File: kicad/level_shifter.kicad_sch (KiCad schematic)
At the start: 22 parts, among them U3 74LVC2T45GT, U4 74LVC2T45GT, U5 74LVC2T45GT

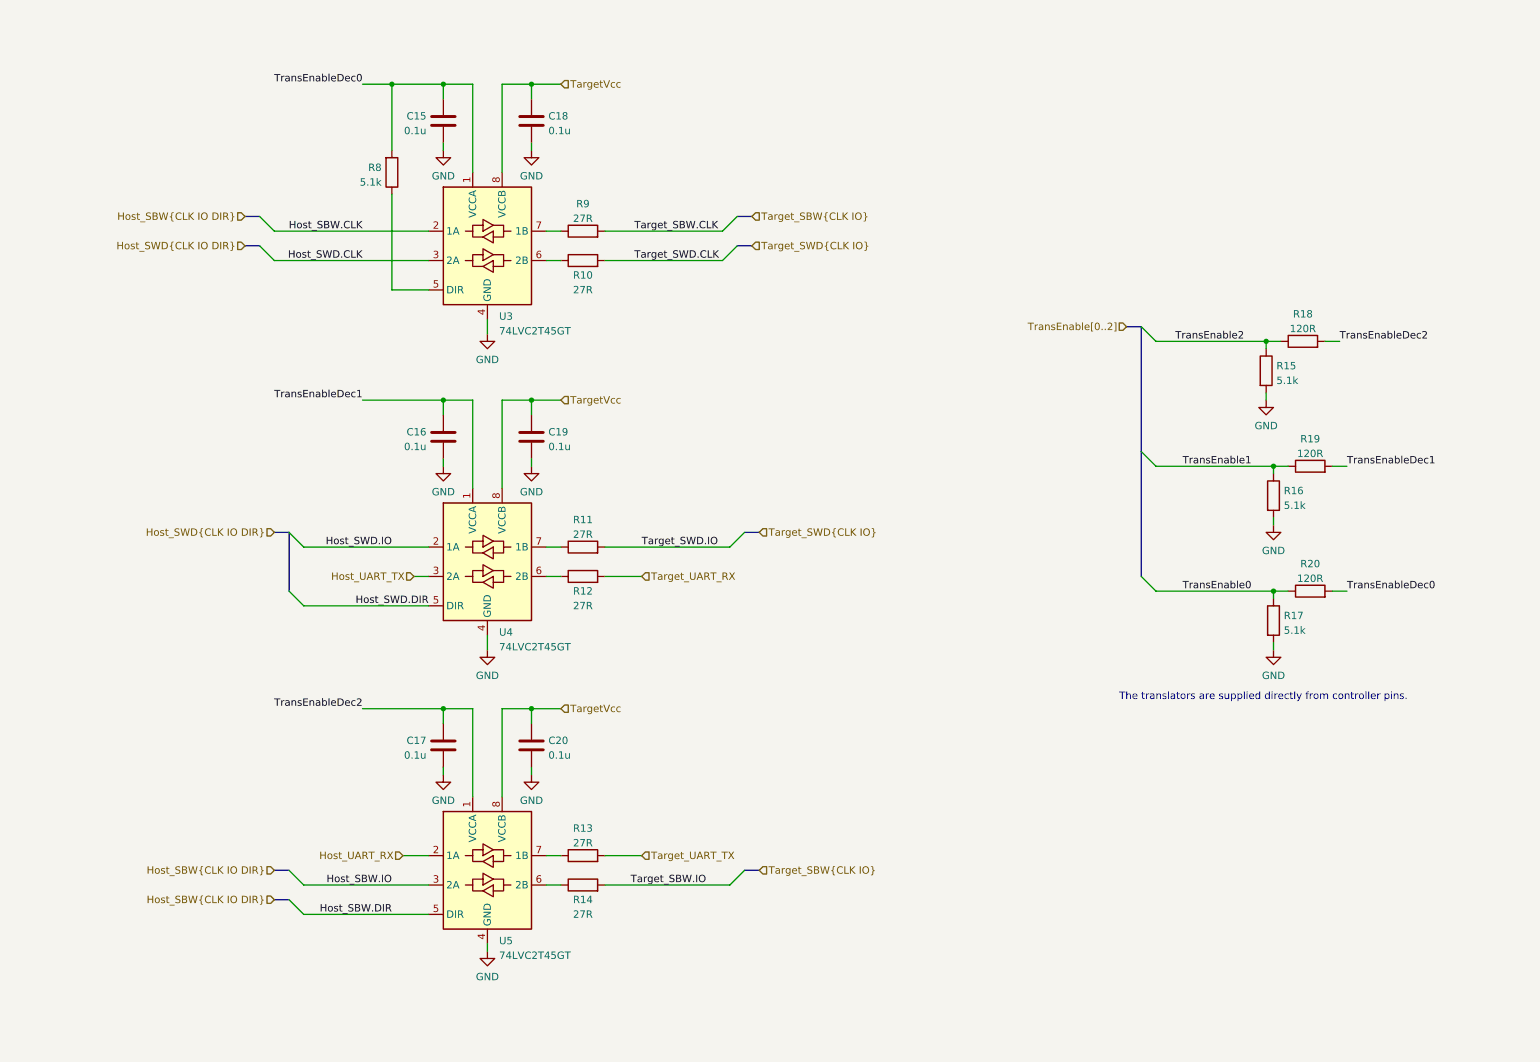
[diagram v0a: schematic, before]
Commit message: add fourth level converter for simultaneous programming + TX/RX
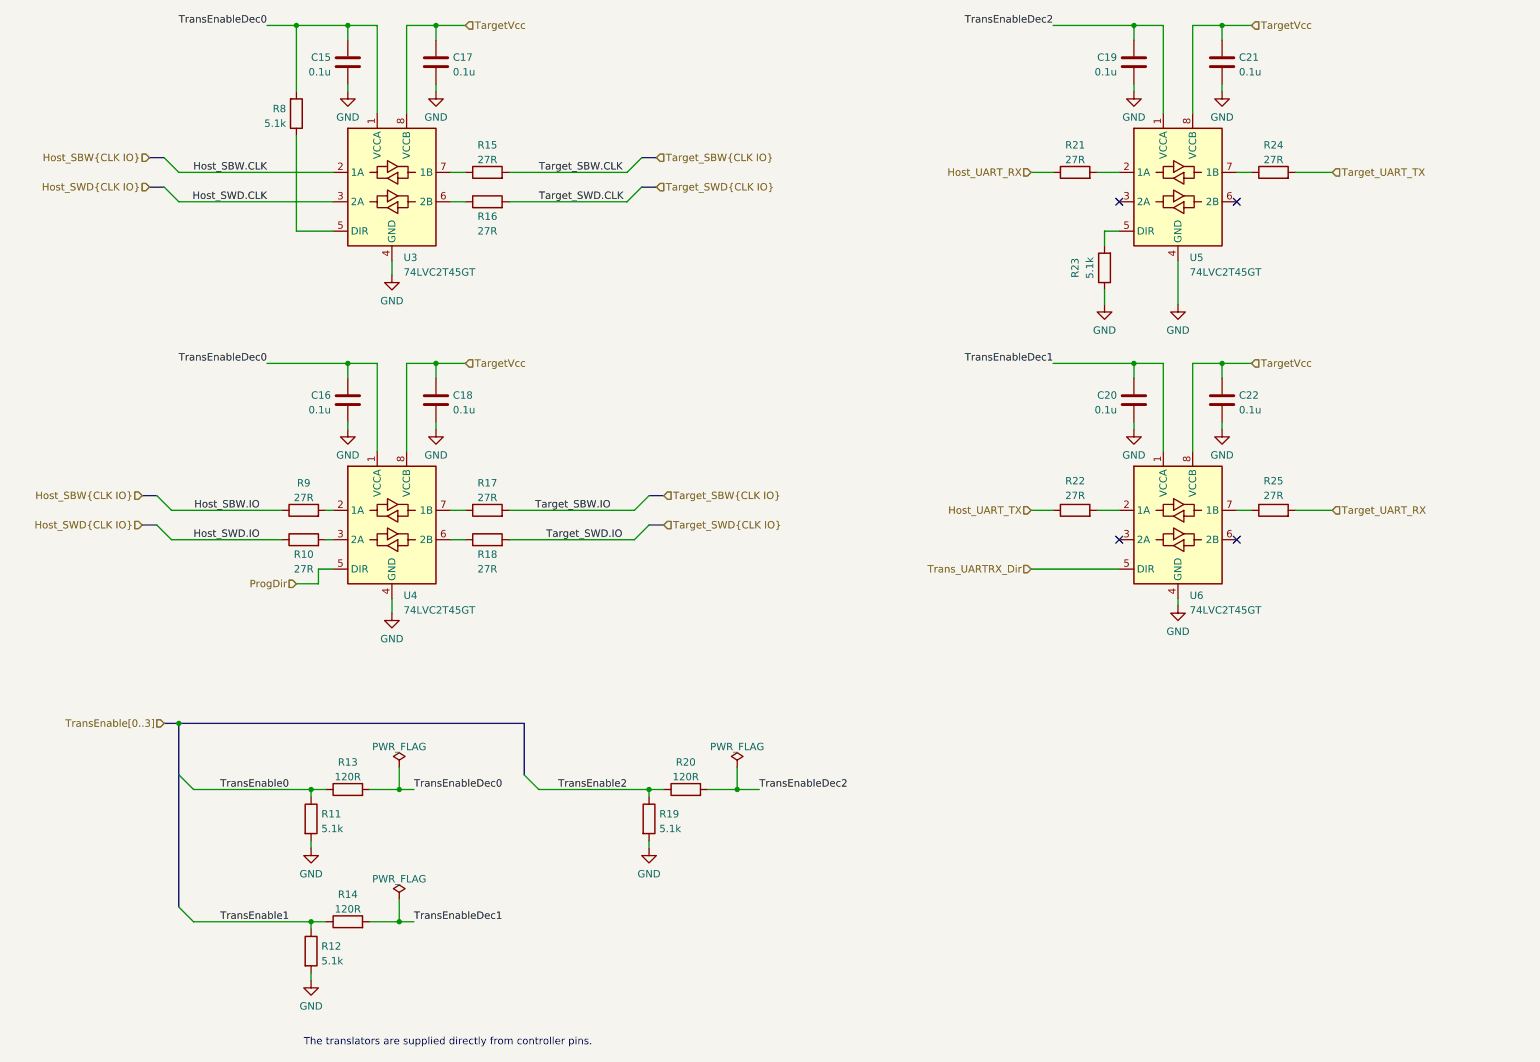
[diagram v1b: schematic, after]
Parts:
- added C20, C22: 0.1u, Capacitor_SMD:C_0402_1005Metric, symbol Device:C
- added R10, R21, R22, R9: 27R, Resistor_SMD:R_0402_1005Metric, symbol Device:R
- added R23: 5.1k, Resistor_SMD:R_0402_1005Metric, symbol Device:R
- added U6: 74LVC2T45GT, riotee:NXP_SOT833-1, symbol riotee:74LVC2T45GT
- renumbered C18 to C17, C19 to C18, C17 to C19, C20 to C21, R17 to R11, R16 to R12, R20 to R13, R19 to R14, R9 to R15, R10 to R16, R11 to R17, R14 to R18, R15 to R19, R18 to R20, R13 to R24, R12 to R25
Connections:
- net GND: now also C20.1, C22.2, R23.1, U6.4 (GND)
- net Host_SBW.IO: now also R9.1; no longer U5.3 (2A)
- net Host_SWD.IO: now also R10.1; no longer U4.2 (1A)
- net Host_UART_RX: now also R21.1; no longer U5.2 (1A)
- net Host_UART_TX: now also R22.1; no longer U4.3 (2A)
- net TargetVcc: now also C22.1, U6.8 (VCCB)
- net Target_SBW.IO: now also R17.2; no longer R18.2
- net Target_SWD.IO: now also R18.2; no longer R17.2
- net TransEnableDec0: now also C16.2, U4.1 (VCCA)
- net TransEnableDec1: now also C20.2, U6.1 (VCCA); no longer C16.2, U4.1 (VCCA)
- net at U5.6 (2B): no longer R18.1
- net at U4.6 (2B): now also R18.1; no longer R25.1
- net Host_SBW.DIR: no longer names the net of U5.5 (DIR)
- net Host_SBW.DIR: now also R23.2
- net Host_SWD.DIR renamed ProgDir
- new net: R21.2, U5.2 (1A)
- new net: R22.2, U6.2 (1A)
- new net: R9.2, U4.2 (1A)
- new net: R25.1, U6.7 (1B)
- new net: R10.2, U4.3 (2A)
- new net Trans_UARTRX_Dir: U6.5 (DIR)
- no-connect marks 0 -> 4
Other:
- moved on the sheet: C15, C16, C17, C18, C19, C21, R11, R12, R13, R14, R15, R16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

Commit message: fix some net names
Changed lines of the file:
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@@
     (effects (font (size 1.27 1.27)) (justify left))
   )
-  (hierarchical_label "TransEnable[0..3]" (shape input) (at 39.37 137.16 180)
+  (hierarchical_label "TransEnable[0..2]" (shape input) (at 39.37 137.16 180)
     (effects (font (size 1.27 1.27)) (justify right))
   )

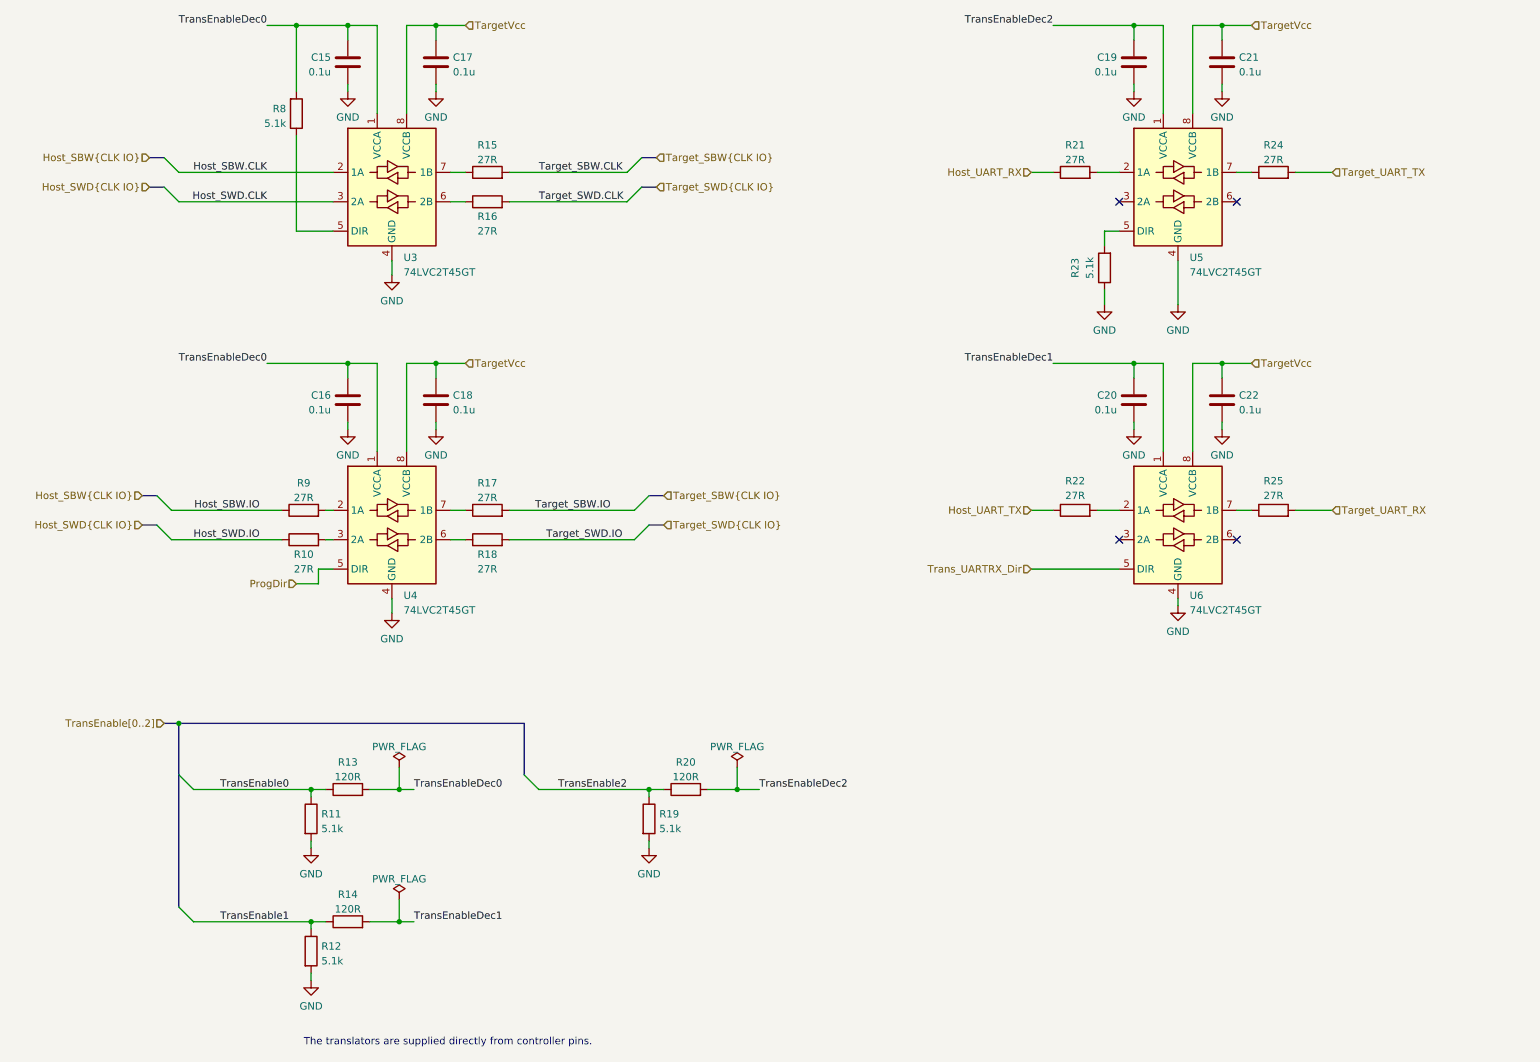
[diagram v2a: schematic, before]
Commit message: adjust values of level translator series resistors
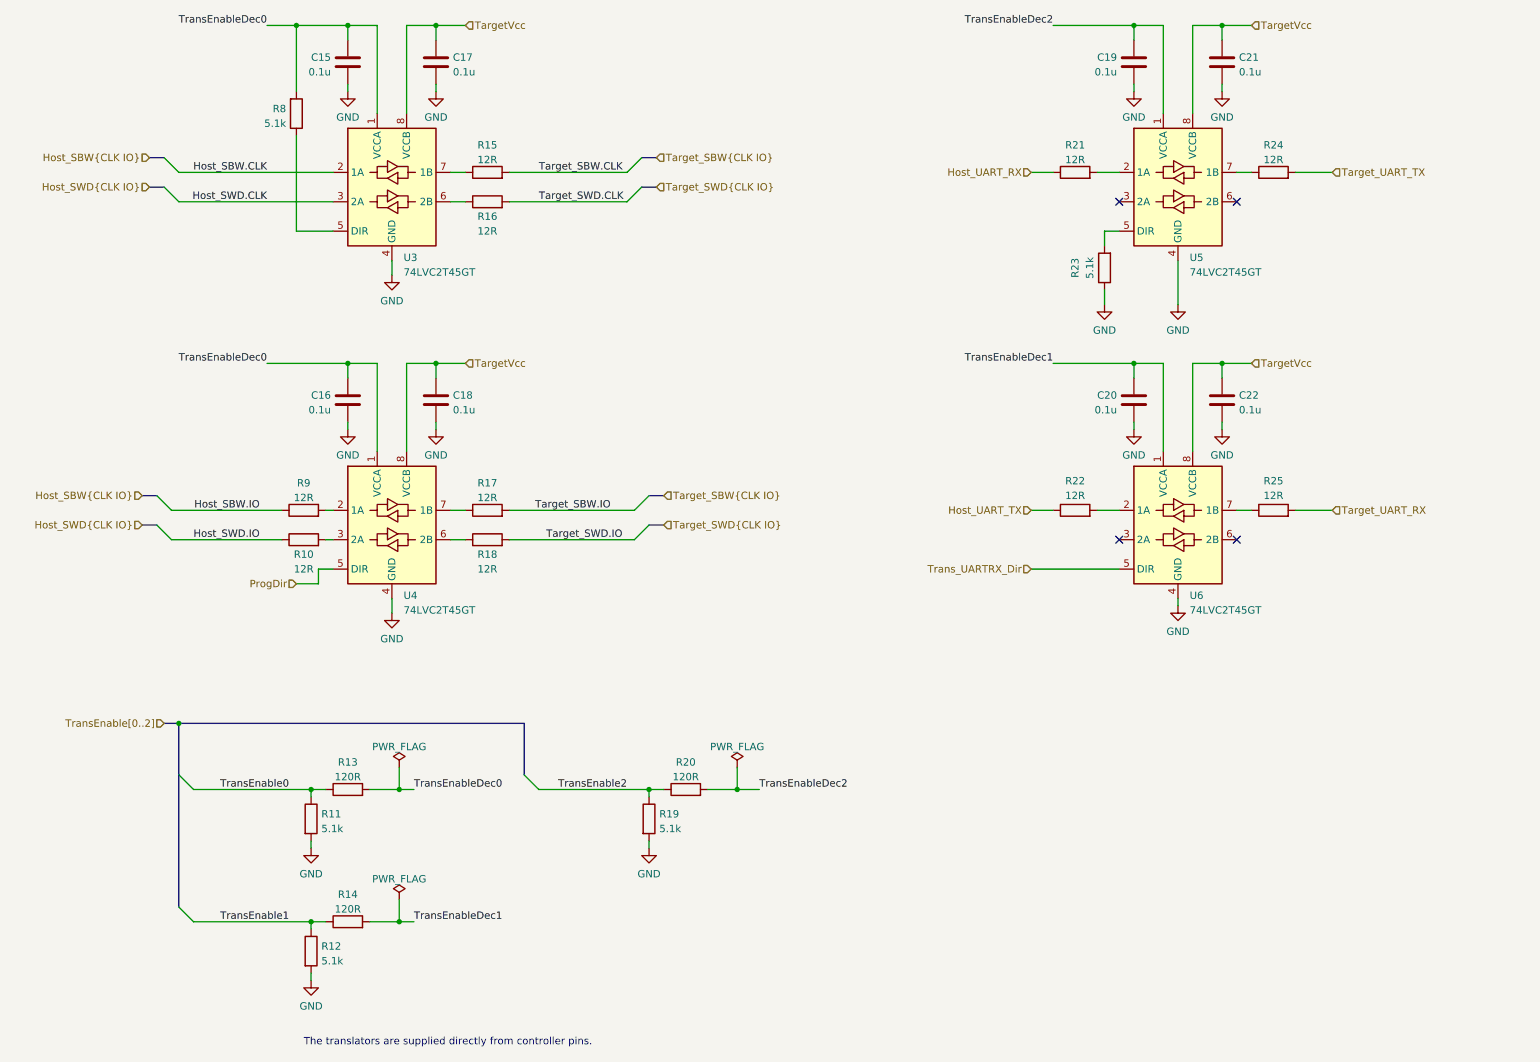
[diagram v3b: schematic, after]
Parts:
- R10, R15, R16, R17, R18, R21, R22, R24, R25, R9: value 27R -> 12R
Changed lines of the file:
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@@
     (in_bom yes) (on_board yes) (fields_autoplaced)
     (property "Reference" "R17" (id 0) (at 95.25 95.6142 90))
-    (property "Value" "27R" (id 1) (at 95.25 98.1511 90))
+    (property "Value" "12R" (id 1) (at 95.25 98.1511 90))
     (property "Footprint" "Resistor_SMD:R_0402_1005Metric" (id 2) (at 95.25 102.108 90)
       (effects (font (size 1.27 1.27)) hide)
@@
     (pin "2")
   )
-  (symbol (lib_name "74LVC2T45GT_2") (lib_id "riotee:74LVC2T45GT") (at 214.63 44.45 0) (unit 1)
+  (symbol (lib_id "riotee:74LVC2T45GT") (at 214.63 44.45 0) (unit 1)
     (in_bom yes) (on_board yes) (fields_autoplaced)
     (property "Reference" "U5" (id 0) (at 216.6494 56.6404 0)
@@
       (effects (font (size 1.27 1.27)) (justify left))
     )
-    (property "Footprint" "riotee:NXP_SOT833-1" (id 2) (at 214.63 66.04 0)
+    (property "Footprint" "riotee:NXP_SOT833-1" (id 2) (at 214.63 67.31 0)
       (effects (font (size 1.27 1.27)) hide)
     )
@@
     (in_bom yes) (on_board yes)
     (property "Reference" "R22" (id 0) (at 196.85 95.2531 90))
-    (property "Value" "27R" (id 1) (at 196.85 97.79 90))
+    (property "Value" "12R" (id 1) (at 196.85 97.79 90))
     (property "Footprint" "Resistor_SMD:R_0402_1005Metric" (id 2) (at 196.85 102.108 90)
       (effects (font (size 1.27 1.27)) hide)
@@
     (in_bom yes) (on_board yes) (fields_autoplaced)
     (property "Reference" "R9" (id 0) (at 63.5 95.6142 90))
-    (property "Value" "27R" (id 1) (at 63.5 98.1511 90))
+    (property "Value" "12R" (id 1) (at 63.5 98.1511 90))
     (property "Footprint" "Resistor_SMD:R_0402_1005Metric" (id 2) (at 63.5 102.108 90)
       (effects (font (size 1.27 1.27)) hide)
@@
     (in_bom yes) (on_board yes) (fields_autoplaced)
     (property "Reference" "R15" (id 0) (at 95.25 37.1942 90))
-    (property "Value" "27R" (id 1) (at 95.25 39.7311 90))
+    (property "Value" "12R" (id 1) (at 95.25 39.7311 90))
     (property "Footprint" "Resistor_SMD:R_0402_1005Metric" (id 2) (at 95.25 43.688 90)
       (effects (font (size 1.27 1.27)) hide)
@@
     (in_bom yes) (on_board yes)
     (property "Reference" "R18" (id 0) (at 95.25 107.95 90))
-    (property "Value" "27R" (id 1) (at 95.25 110.4869 90))
+    (property "Value" "12R" (id 1) (at 95.25 110.4869 90))
     (property "Footprint" "Resistor_SMD:R_0402_1005Metric" (id 2) (at 95.25 107.188 90)
       (effects (font (size 1.27 1.27)) hide)
@@
     (in_bom yes) (on_board yes)
     (property "Reference" "R25" (id 0) (at 231.14 95.2531 90))
-    (property "Value" "27R" (id 1) (at 231.14 97.79 90))
+    (property "Value" "12R" (id 1) (at 231.14 97.79 90))
     (property "Footprint" "Resistor_SMD:R_0402_1005Metric" (id 2) (at 231.14 102.108 90)
       (effects (font (size 1.27 1.27)) hide)
@@
     (in_bom yes) (on_board yes) (fields_autoplaced)
     (property "Reference" "R21" (id 0) (at 196.85 37.1942 90))
-    (property "Value" "27R" (id 1) (at 196.85 39.7311 90))
+    (property "Value" "12R" (id 1) (at 196.85 39.7311 90))
     (property "Footprint" "Resistor_SMD:R_0402_1005Metric" (id 2) (at 196.85 43.688 90)
       (effects (font (size 1.27 1.27)) hide)
@@
     (pin "2")
   )
-  (symbol (lib_name "74LVC2T45GT_1") (lib_id "riotee:74LVC2T45GT") (at 78.74 102.87 0) (unit 1)
+  (symbol (lib_id "riotee:74LVC2T45GT") (at 78.74 102.87 0) (unit 1)
     (in_bom yes) (on_board yes) (fields_autoplaced)
     (property "Reference" "U4" (id 0) (at 80.7594 115.0604 0)
@@
       (effects (font (size 1.27 1.27)) (justify left))
     )
-    (property "Footprint" "riotee:NXP_SOT833-1" (id 2) (at 78.74 124.46 0)
+    (property "Footprint" "riotee:NXP_SOT833-1" (id 2) (at 78.74 125.73 0)
       (effects (font (size 1.27 1.27)) hide)
     )
@@
     (pin "1")
   )
-  (symbol (lib_name "74LVC2T45GT_3") (lib_id "riotee:74LVC2T45GT") (at 214.63 102.87 0) (unit 1)
+  (symbol (lib_id "riotee:74LVC2T45GT") (at 214.63 102.87 0) (unit 1)
     (in_bom yes) (on_board yes) (fields_autoplaced)
     (property "Reference" "U6" (id 0) (at 216.6494 115.0604 0)
@@
       (effects (font (size 1.27 1.27)) (justify left))
     )
-    (property "Footprint" "riotee:NXP_SOT833-1" (id 2) (at 214.63 124.46 0)
+    (property "Footprint" "riotee:NXP_SOT833-1" (id 2) (at 214.63 125.73 0)
       (effects (font (size 1.27 1.27)) hide)
     )
@@
     (in_bom yes) (on_board yes) (fields_autoplaced)
     (property "Reference" "R24" (id 0) (at 231.14 37.1942 90))
-    (property "Value" "27R" (id 1) (at 231.14 39.7311 90))
+    (property "Value" "12R" (id 1) (at 231.14 39.7311 90))
     (property "Footprint" "Resistor_SMD:R_0402_1005Metric" (id 2) (at 231.14 43.688 90)
       (effects (font (size 1.27 1.27)) hide)
@@
     (in_bom yes) (on_board yes)
     (property "Reference" "R16" (id 0) (at 95.25 49.53 90))
-    (property "Value" "27R" (id 1) (at 95.25 52.0669 90))
+    (property "Value" "12R" (id 1) (at 95.25 52.0669 90))
     (property "Footprint" "Resistor_SMD:R_0402_1005Metric" (id 2) (at 95.25 48.768 90)
       (effects (font (size 1.27 1.27)) hide)
@@
     (in_bom yes) (on_board yes)
     (property "Reference" "R10" (id 0) (at 63.5 107.95 90))
-    (property "Value" "27R" (id 1) (at 63.5 110.4869 90))
+    (property "Value" "12R" (id 1) (at 63.5 110.4869 90))
     (property "Footprint" "Resistor_SMD:R_0402_1005Metric" (id 2) (at 63.5 107.188 90)
       (effects (font (size 1.27 1.27)) hide)
